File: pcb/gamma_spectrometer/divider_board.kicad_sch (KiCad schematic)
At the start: 36 parts, among them Q401 MMBTA42, Q402 MMBTA42, Q403 MMBTA42, U401 AD8000YRDZ-REEL

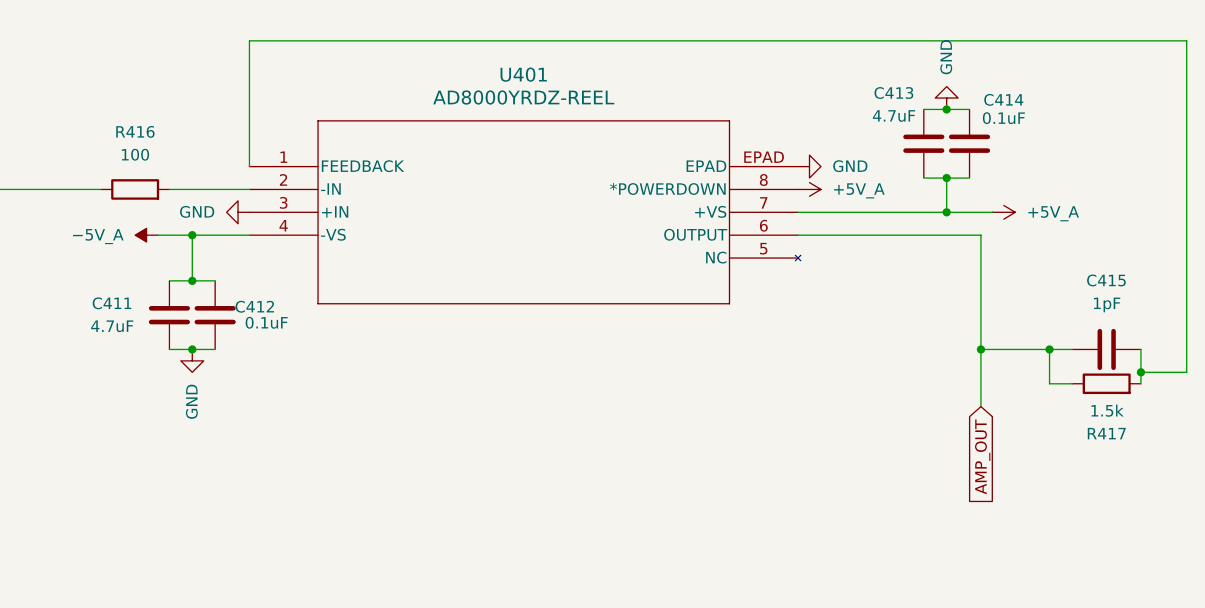
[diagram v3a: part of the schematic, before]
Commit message: fix(divider): AD8000 ОС на −IN (была OUT↔FB, петля разомкнута) + правило #11
Инженер нашёл на живой схеме: Rfb(R417)/Cfb(C415) стояли между OUTPUT(6) и
FEEDBACK(1). У AD8000 пин FB внутри = выход (даташит «Low Distortion Pinout»),
поэтому оба конца сидели на выходном узле → на Rfb 0 В, петля ОС разомкнута,
−IN без обратной связи → ОУ в насыщении, усиления ×−15 нет.

Исправлено (схема + нетлист): Rfb‖Cfb теперь между FB(1) и −IN(2); выход (6)
= AMP_OUT (U.FL + шейпер). Проверено по нетлисту пин-в-пин: gain = −Rfb/Rg = −15.

- cheatsheet_mistakes.md: правило #11 (ОУ с FB-пином: Rfb на −IN; сверять пины
  с даташитом, не только ERC; разбор почему 3 проверки пропустили).
- divider_board.md, CLAUDE.md: топология узла приведена к FB↔−IN.

PCB делителя ещё не разведён → физической правки платы не требуется.

Co-Authored-By: Claude Opus 4.8 <noreply@anthropic.com>
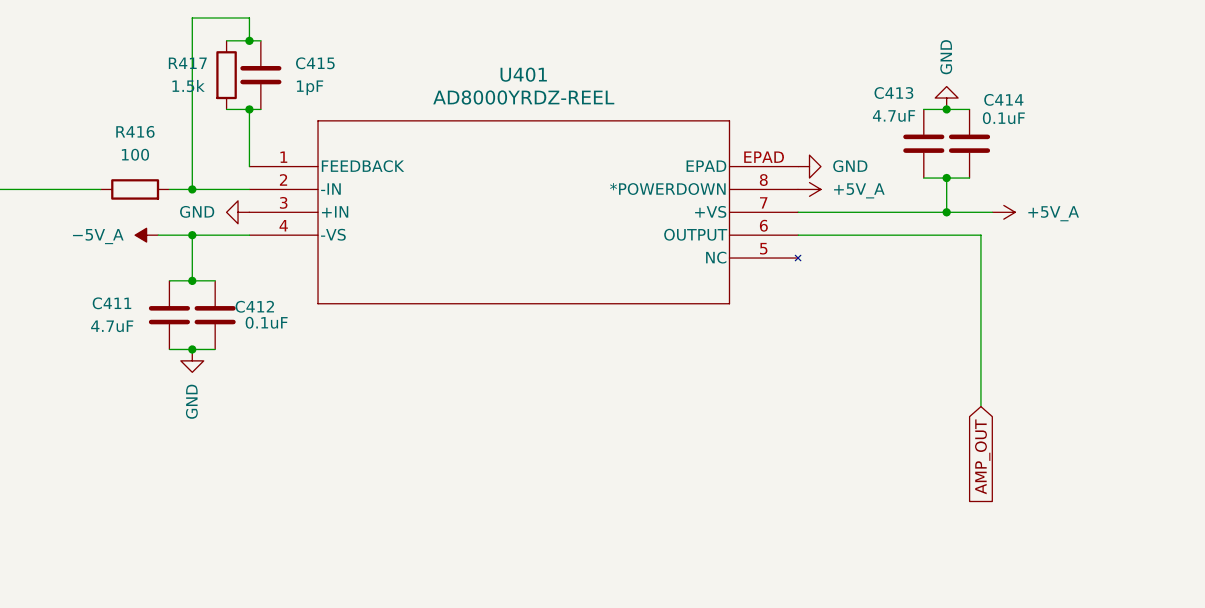
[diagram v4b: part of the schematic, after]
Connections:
- net AMP_OUT: no longer C415.1, R417.1
- net at R417.2, U401.1 (FEEDBACK): now also C415.1; no longer C415.2
- net at R416.2, U401.2 (-IN): now also C415.2, R417.1
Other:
- moved on the sheet: C415, R417
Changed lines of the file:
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@@
 	)
 	(junction
-		(at 285.75 53.34)
-		(diameter 0)
-		(color 0 0 0 0)
-	)
-	(junction
 		(at 180.34 38.1)
 		(diameter 0)
@@
 	)
 	(junction
-		(at 275.59 50.8)
+		(at 186.69 16.51)
 		(diameter 0)
 		(color 0 0 0 0)
@@
 	)
 	(junction
+		(at 186.69 24.13)
+		(diameter 0)
+		(color 0 0 0 0)
+	)
+	(junction
 		(at 110.49 43.18)
 		(diameter 0)
@@
 	)
 	(junction
-		(at 267.97 50.8)
-		(diameter 0)
-		(color 0 0 0 0)
-	)
-	(junction
 		(at 102.87 73.66)
 		(diameter 0)
@@
 	)
 	(junction
+		(at 180.34 33.02)
+		(diameter 0)
+		(color 0 0 0 0)
+	)
+	(junction
 		(at 139.7 73.66)
 		(diameter 0)
@@
 	(wire
 		(pts
-			(xy 267.97 50.8) (xy 267.97 38.1)
+			(xy 267.97 38.1) (xy 267.97 57.15)
 		)
 		(stroke
@@
 	(wire
 		(pts
-			(xy 120.65 73.66) (xy 119.38 73.66)
+			(xy 186.69 16.51) (xy 187.96 16.51)
 		)
 		(stroke
@@
 	(wire
 		(pts
-			(xy 177.8 33.02) (xy 186.69 33.02)
+			(xy 120.65 73.66) (xy 119.38 73.66)
 		)
 		(stroke
@@
 	(wire
 		(pts
-			(xy 285.75 53.34) (xy 285.75 54.61)
+			(xy 177.8 33.02) (xy 180.34 33.02)
 		)
 		(stroke
@@
 	(wire
 		(pts
-			(xy 290.83 53.34) (xy 290.83 16.51)
-		)
-		(stroke
-			(width 0)
-			(type default)
-		)
-	)
-	(wire
-		(pts
 			(xy 148.59 53.34) (xy 148.59 73.66)
 		)
@@
 	(wire
 		(pts
+			(xy 184.15 24.13) (xy 186.69 24.13)
+		)
+		(stroke
+			(width 0)
+			(type default)
+		)
+	)
+	(wire
+		(pts
 			(xy 95.25 73.66) (xy 95.25 81.28)
 		)
@@
 	(wire
 		(pts
-			(xy 124.46 46.99) (xy 125.73 46.99)
+			(xy 186.69 24.13) (xy 187.96 24.13)
 		)
 		(stroke
@@
 	(wire
 		(pts
-			(xy 124.46 53.34) (xy 124.46 46.99)
+			(xy 124.46 46.99) (xy 125.73 46.99)
 		)
 		(stroke
@@
 	(wire
 		(pts
-			(xy 147.32 73.66) (xy 148.59 73.66)
+			(xy 124.46 53.34) (xy 124.46 46.99)
 		)
 		(stroke
@@
 	(wire
 		(pts
-			(xy 148.59 40.64) (xy 148.59 53.34)
+			(xy 147.32 73.66) (xy 148.59 73.66)
 		)
 		(stroke
@@
 	(wire
 		(pts
-			(xy 129.54 68.58) (xy 129.54 73.66)
+			(xy 148.59 40.64) (xy 148.59 53.34)
 		)
 		(stroke
@@
 	(wire
 		(pts
-			(xy 186.69 16.51) (xy 186.69 30.48)
+			(xy 129.54 68.58) (xy 129.54 73.66)
 		)
 		(stroke
@@
 	(wire
 		(pts
-			(xy 275.59 50.8) (xy 267.97 50.8)
-		)
-		(stroke
-			(width 0)
-			(type default)
-		)
-	)
-	(wire
-		(pts
 			(xy 110.49 38.1) (xy 110.49 43.18)
 		)
@@
 	(wire
 		(pts
-			(xy 275.59 50.8) (xy 278.13 50.8)
+			(xy 180.34 33.02) (xy 186.69 33.02)
 		)
 		(stroke
@@
 	(wire
 		(pts
-			(xy 290.83 16.51) (xy 186.69 16.51)
+			(xy 186.69 13.97) (xy 180.34 13.97)
 		)
 		(stroke
@@
 	(wire
 		(pts
-			(xy 285.75 50.8) (xy 285.75 53.34)
+			(xy 80.01 73.66) (xy 80.01 34.29)
 		)
 		(stroke
@@
 	(wire
 		(pts
-			(xy 80.01 73.66) (xy 80.01 34.29)
+			(xy 186.69 16.51) (xy 186.69 13.97)
 		)
 		(stroke
@@
 	(wire
 		(pts
-			(xy 275.59 54.61) (xy 278.13 54.61)
+			(xy 87.63 73.66) (xy 87.63 35.56)
 		)
 		(stroke
@@
 	(wire
 		(pts
-			(xy 87.63 73.66) (xy 87.63 35.56)
+			(xy 95.25 73.66) (xy 95.25 35.56)
 		)
 		(stroke
@@
 	(wire
 		(pts
-			(xy 95.25 73.66) (xy 95.25 35.56)
+			(xy 134.62 45.72) (xy 134.62 53.34)
 		)
 		(stroke
@@
 	(wire
 		(pts
-			(xy 134.62 45.72) (xy 134.62 53.34)
+			(xy 125.73 35.56) (xy 125.73 43.18)
 		)
 		(stroke
@@
 	(wire
 		(pts
-			(xy 290.83 53.34) (xy 285.75 53.34)
+			(xy 109.22 34.29) (xy 109.22 31.75)
 		)
 		(stroke
@@
 	(wire
 		(pts
-			(xy 125.73 35.56) (xy 125.73 43.18)
+			(xy 148.59 33.02) (xy 170.18 33.02)
 		)
 		(stroke
@@
 	(wire
 		(pts
-			(xy 109.22 34.29) (xy 109.22 31.75)
+			(xy 80.01 34.29) (xy 91.44 34.29)
 		)
 		(stroke
@@
 	(wire
 		(pts
-			(xy 148.59 33.02) (xy 170.18 33.02)
+			(xy 186.69 30.48) (xy 186.69 24.13)
 		)
 		(stroke
@@
 	(wire
 		(pts
-			(xy 80.01 34.29) (xy 91.44 34.29)
+			(xy 184.15 16.51) (xy 186.69 16.51)
 		)
 		(stroke
@@
 	(wire
 		(pts
-			(xy 275.59 54.61) (xy 275.59 50.8)
+			(xy 180.34 13.97) (xy 180.34 33.02)
 		)
 		(stroke
@@
 	(wire
 		(pts
-			(xy 267.97 50.8) (xy 267.97 57.15)
-		)
-		(stroke
-			(width 0)
-			(type default)
-		)
-	)
-	(wire
-		(pts
 			(xy 125.73 46.99) (xy 125.73 43.18)
 		)
@@
 	(symbol
 		(lib_id "Device:R")
-		(at 281.94 54.61 90)
+		(at 184.15 20.32 0)
 		(unit 1)
 		(exclude_from_sim no)
@@
 		(dnp no)
 		(property "Reference" "R417"
-			(at 281.94 60.198 90)
+			(at 179.832 19.05 0)
 			(effects
 				(font
@@
 		)
 		(property "Value" "1.5k"
-			(at 281.94 57.658 90)
+			(at 179.832 21.59 0)
 			(effects
 				(font
@@
 		)
 		(property "Footprint" "Resistor_SMD:R_0603_1608Metric_Pad0.98x0.95mm_HandSolder"
-			(at 281.94 56.388 90)
+			(at 182.372 20.32 90)
 			(effects
 				(font
@@
 		)
 		(property "Datasheet" "~"
-			(at 281.94 54.61 0)
+			(at 184.15 20.32 0)
 			(effects
 				(font
@@
 		)
 		(property "Description" "Resistor"
-			(at 281.94 54.61 0)
+			(at 184.15 20.32 0)
 			(effects
 				(font
@@
 		)
 		(property "KLC_S3.3" ""
-			(at 281.94 54.61 90)
+			(at 184.15 20.32 90)
 			(effects
 				(font
@@
 		)
 		(property "KLC_S4.1" ""
-			(at 281.94 54.61 90)
+			(at 184.15 20.32 90)
 			(effects
 				(font
@@
 		)
 		(property "PN" "RC0603FR-071K5L"
-			(at 281.94 54.61 90)
+			(at 184.15 20.32 90)
 			(effects
 				(font
@@
 		)
 		(property "Ссылка на покупку " "https://www.electronshik.ru/item/YAG/RC0603FR-071K5L"
-			(at 281.94 54.61 90)
+			(at 184.15 20.32 90)
 			(effects
 				(font
@@
 	(symbol
 		(lib_id "Device:C")
-		(at 281.94 50.8 90)
+		(at 187.96 20.32 180)
 		(unit 1)
 		(exclude_from_sim no)
@@
 		(fields_autoplaced yes)
 		(property "Reference" "C415"
-			(at 281.94 43.18 90)
+			(at 191.77 19.0499 0)
 			(effects
 				(font
 					(size 1.27 1.27)
 				)
+				(justify right)
 			)
 		)
 		(property "Value" "1pF"
-			(at 281.94 45.72 90)
+			(at 191.77 21.5899 0)
 			(effects
 				(font
 					(size 1.27 1.27)
 				)
+				(justify right)
 			)
 		)
 		(property "Footprint" "Capacitor_SMD:C_0402_1005Metric_Pad0.74x0.62mm_HandSolder"
-			(at 285.75 49.8348 0)
+			(at 186.9948 16.51 0)
 			(effects
 				(font
@@
 		)
 		(property "Datasheet" "~"
-			(at 281.94 50.8 0)
+			(at 187.96 20.32 0)
 			(effects
 				(font
@@
 		)
 		(property "Description" "Unpolarized capacitor"
-			(at 281.94 50.8 0)
+			(at 187.96 20.32 0)
 			(effects
 				(font
@@
 		)
 		(property "KLC_S3.3" ""
-			(at 281.94 50.8 90)
+			(at 187.96 20.32 90)
 			(effects
 				(font
@@
 		)
 		(property "KLC_S4.1" ""
-			(at 281.94 50.8 90)
+			(at 187.96 20.32 90)
 			(effects
 				(font
@@
 		)
 		(property "PN" "GRM1555C1H1R0WA01D"
-			(at 281.94 50.8 90)
+			(at 187.96 20.32 90)
 			(effects
 				(font
@@
 		)
 		(property "Ссылка на покупку " "https://www.electronshik.ru/item/MUR/GRM1555C1H1R0WA01D"
-			(at 281.94 50.8 90)
+			(at 187.96 20.32 90)
 			(effects
 				(font

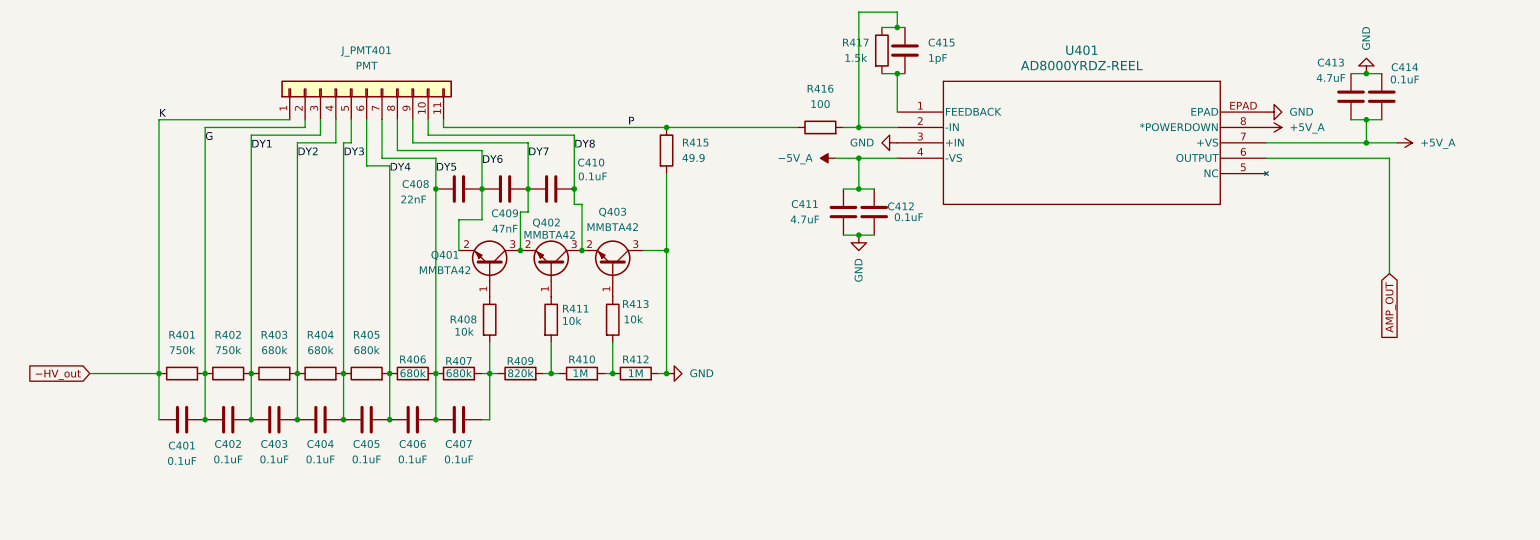
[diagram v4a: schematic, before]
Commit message: divider: активный делитель пересобран по Fig 5-15 + валидирован
Буферная секция переделана по Hamamatsu PMT Handbook (Fig 5-15, стр.108):
цепочка через диноды, транзисторы смещены током делителя, защитные диоды B-E.

Проверено simulation/sim_div_final.cir (-1500В, MMBTA42+1N4148 модели):
- смещение Q401-403: Ic ≈ 96 мкА (было 0.19 нА — изъян закрыт), ток делителя 195 мкА.
- распределение: K-G/G-Dy1 146В, Dy1-Dy5 132В, Dy6-Dy7 157В, Dy7-Dy8 197В,
  Dy8-GND 198В (тейпер восстановлен), сумма 1500В.
- диоды D401-403 (1N4148W, B-E клампы) в норме закрыты (~9нА), не трогают смещение.

Номиналы поздней секции: R407=1.3М, R408=1.3М, R409=1.6М, R410=2М, R412=2М (1206 1%).
Капы только Dy6-Dy8 (C408/409/410 = 22/47/100 нФ).

docs: divider_board.md — таблица/буферы переписаны под валидированную схему;
divider_rework.md — статус «пересобрано». Остаётся вход → ADA4817 TIA.

Co-Authored-By: Claude Opus 4.8 <noreply@anthropic.com>
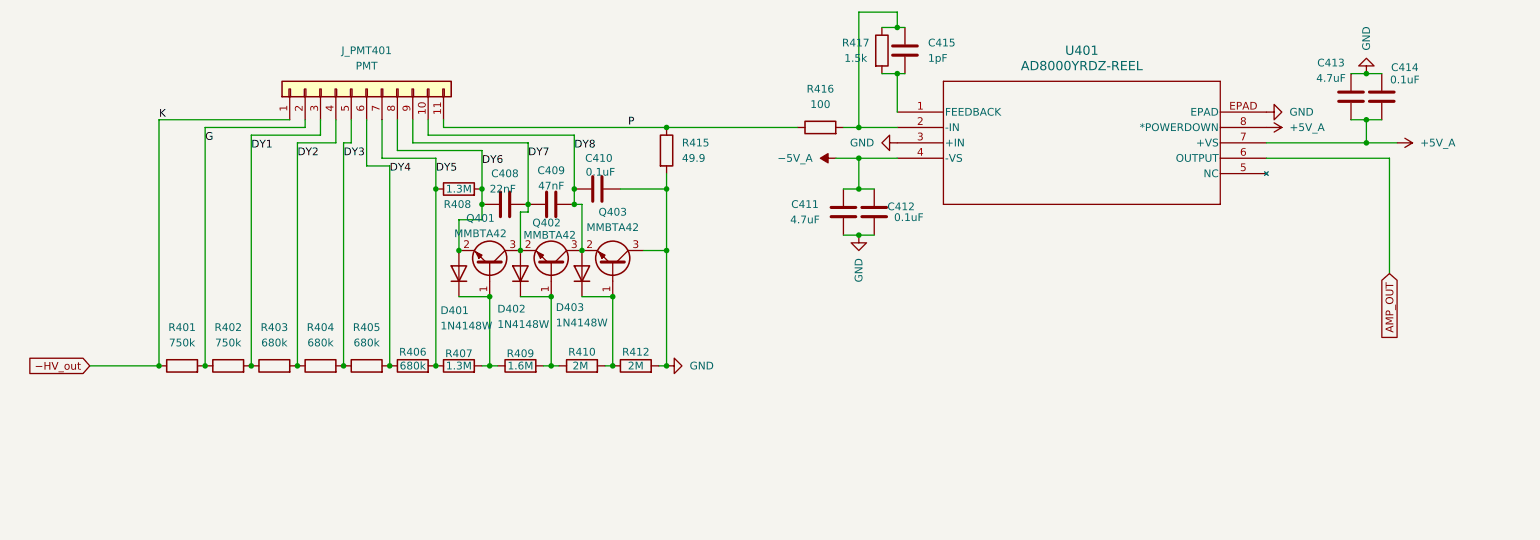
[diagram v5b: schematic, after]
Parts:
- removed C401, C402, C403, C404, C405, C406, C407: 0.1uF, Capacitor_SMD:C_1812_4532Metric_Pad1.57x3.40mm_HandSolder, symbol Device:C
- removed R411, R413: 10k, Resistor_SMD:R_0603_1608Metric_Pad0.98x0.95mm_HandSolder, symbol Device:R
- added D401, D402, D403: 1N4148W, Diode_SMD:D_SOD-123, symbol Diode:1N4148W
- R407: value 680k -> 1.3M; PN RC1206FR-07680KL -> RC1206FR-071M3L; Ссылка на покупку  https://www.electronshik.ru/item/YAG/RC1206FR-07680KL -> https://www.electronshik.ru/item/YAG/RC1206FR-071M3L
- R408: value 10k -> 1.3M; footprint Resistor_SMD:R_0603_1608Metric_Pad0.98x0.95mm_HandSolder -> Resistor_SMD:R_1206_3216Metric_Pad1.30x1.75mm_HandSolder; PN RC0603FR-0710KL -> RC1206FR-071M3L; Ссылка на покупку  https://www.electronshik.ru/item/YAG/RC0603FR-0710KL -> https://www.electronshik.ru/item/YAG/RC1206FR-071M3L
- R409: value 820k -> 1.6M; PN RC1206FR-07820KL -> RC1206FR-071M6L; Ссылка на покупку  https://www.electronshik.ru/item/YAG/RC1206FR-07820KL -> https://www.electronshik.ru/item/YAG/RC1206FR-071M6L
- R410, R412: value 1M -> 2M; PN RC1206FR-071ML -> RC1206FR-072ML; Ссылка на покупку  https://www.electronshik.ru/item/YAG/RC1206FR-071ML -> https://www.electronshik.ru/item/YAG/RC1206FR-072ML
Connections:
- net DY5: now also R408.1; no longer C408.1
- net DY6: now also C408.1, R408.2, D401.2 (A); no longer C408.2, C409.1
- net DY7: now also C408.2, C409.1, D402.2 (A); no longer C409.2, C410.1
- net DY8: now also C409.2, C410.1, D403.2 (A); no longer C410.2
- net GND: now also C410.2
- net at R407.2, R409.1: now also Q401.1 (B), D401.1 (K); no longer R408.2
- net at R410.2, R412.1: now also Q403.1 (B), D403.1 (K)
- net at R409.2, R410.1: now also Q402.1 (B), D402.1 (K)
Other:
- moved on the sheet: C408, C409, C410, R401, R402, R403, R404, R405, R406, R407, R409, R410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

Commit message: divider: вход на ADA4817 TIA + единая модель всей платы делителя
Вход переведён с AD8000-инвертора на ADA4817-1ARDZ (U402) как TIA:
- анод P напрямую на −IN (виртуальная земля), R415/R416 убраны;
- Rf=R417=499, Cf=C415=4.7пФ между FB и −IN; +IN→AGND, PD→+5V_A, EPAD→AGND.

Единая модель simulation/sim_divider_complete.cir (делитель −1500В + буферы +
диоды + TIA, транзиент с импульсом ФЭУ) подтверждает весь тракт:
- диноды смещены (DY6/7/8 = −552/−395/−198В), буферы ~96мкА, ток 195мкА;
- анод на 0В (виртуальная земля); импульс 3.5 МэВ (4.97мА) → AMP_OUT 2.47В,
  Zt=499Ω, без клиппинга;
- шум TIA 76.9 мкВ (−18% vs AD8000), sim_tia_real Cf→4.7п.

docs: divider_board.md — входная секция переписана под TIA (U402), таблица
компонентов обновлена; CLAUDE.md #7 → «делитель пересобран целиком»;
divider_rework.md → все пункты закрыты. Осталось по делителю — разводка PCB.

Co-Authored-By: Claude Opus 4.8 <noreply@anthropic.com>
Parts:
- removed R415: 49.9, Resistor_SMD:R_0603_1608Metric_Pad0.98x0.95mm_HandSolder, symbol Device:R
- removed R416: 100, Resistor_SMD:R_0603_1608Metric_Pad0.98x0.95mm_HandSolder, symbol Device:R
- removed U401: AD8000YRDZ-REEL, посадочные места:RD_8_1_ADI-M, symbol AD8000YRDZ:AD8000YRDZ-REEL
- added U402: ADA4817-1ARDZ, RD_8_1_ADI, symbol ADA4817-1ARDZ:ADA4817-1ARDZ
- C415: value 1pF -> 4.7pF; PN GRM1555C1H1R0WA01D -> GRM1555C1H4R7WA01D; Ссылка на покупку  https://www.electronshik.ru/item/MUR/GRM1555C1H1R0WA01D -> https://www.electronshik.ru/item/MUR/GRM1555C1H4R7WA01D
- R417: value 1.5k -> 499; PN RC0603FR-071K5L -> RC1206FR-07499RL; Ссылка на покупку  https://www.electronshik.ru/item/YAG/RC0603FR-071K5L -> https://www.electronshik.ru/item/YAG/RC1206FR-07499RL
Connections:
- net +5V_A: now also U402.7 (+VS), U402.8 (PD*)
- net AMP_OUT: now also U402.6 (OUT)
- net GND: now also U402.3 (+IN), U402.EPAD (EP(GND))
- net P: now also C415.1, R417.2, U402.2 (-IN)
- net −5V_A: now also U402.4 (-VS)
- net FeedBack: now reaches C415.2, R417.1
- net FeedBack: now also U402.1 (FB)
- no-connect marks 0 -> 1
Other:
- moved on the sheet: C408, C409, C410, C411, C412, C413, C414, C415, D401, D402, D403, J_PMT401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

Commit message: pcb: ВВ-зазоры 3 мм/кВ правилами DRC + 2 слоя + разводка делителя
Плата переведена 4 -> 2 слоя (ЛУТ-прототипы): на In1/In2 разводки не было,
удалены только зоны, связность не изменилась (178 несоединённых до и после).
Стек F.Cu / core FR4 1.51 / B.Cu = 1.60 мм. Побочно снят риск: под -1500 В
лежала сплошная земля через препрег 0.1 мм (15 кВ/мм), стало 0.99 кВ/мм.

Нормы ВВ-зазоров заданы правилами DRC (gamma_spectrometer.kicad_dru):
49 правил "ВВ-цепь <-> GND" по 3 мм на 1 кВ + 12 исключений. Потенциалы
посчитаны из топологии: рабочая точка делителя, порядок лестницы CW по
диодам (8 ступеней по 189 В), падения на выходном RC, цепочки ОС и монитора.
Зазоры 4.54 мм (CW_out, 1514 В) ... 0.43 мм. Ограничивают только пару с GND —
между соседними ступенями ВВ разность 150-190 В (принцип градиента).

Исключения: 12 компонентов по схеме соединяют ВВ-узел с землёй (T201, C210,
D205, C410, R412, C13b-C18b201, Q403). У них зазор задан корпусом детали и
перемещением не лечится; прочность держит рабочее напряжение компонента.
R412 при этом на 98% от рейтинга (196 В при 200 В) — кандидат на деление
на два по 1 МОм.

Итог: ВВ-нарушений 357 -> 0, всего 774 -> 416, категория clearance пуста.

Расстановка:
- контуры МК (240,100) и делителя (310,100), стойки GND на всех 4 платах
- J_PMT401 на делителе, поворот -69° подобран перебором по ВВ-зазорам
  (узкое место Dy7: 1.74 мм при требуемых 0.79, минимальный запас +0.95)
- межплатные посадки выровнены на дугу R=20 и соосны: -HV_out 72°, AMP_OUT 325°
- на МК цанга -HV_out заменена сквозным отверстием Ø5 NPTH (H_HV301):
  провод -ВВ идёт мимо платы МК, как и задумано в доках
- шина скопирована с USB на делитель; board_only всем 43 механическим футпринтам
- удалено 13 футпринтов старого делителя (вкл. дубль R408) и 10 GND-виа
- проектная копия футпринта USB-C с падами экрана 25-28 вместо S1
  (экран разъёма висел без цепи)

Симуляции:
- найдена недостоверная метрика пиковости в sim_tia_stab.cir (делила дБ на дБ):
  рапортовала -49.7 дБ там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
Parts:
- J_PMT401: footprint (none) -> посадочные места:J_PMT401_R1307-01
- U402: footprint RD_8_1_ADI -> посадочные места:RD_8_1_ADI-M
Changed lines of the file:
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@@
 			)
 		)
-		(property "Footprint" "RD_8_1_ADI"
+		(property "Footprint" "посадочные места:RD_8_1_ADI-M"
 			(at 200.66 43.18 0)
 			(effects
@@
 			)
 		)
-		(property "Footprint" ""
+		(property "Footprint" "посадочные места:J_PMT401_R1307-01"
 			(at 99.06 41.91 0)
 			(effects
